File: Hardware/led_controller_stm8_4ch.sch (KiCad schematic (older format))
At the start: 27 parts, among them J1 LEDS, J2 STM8_Prog_Conn, J3 EXT_BTN, Q1 2N7002, Q2 2N7002, Q3 2N7002, Q4 2N7002, SW1 SW_Push, U1 STM8S103F3

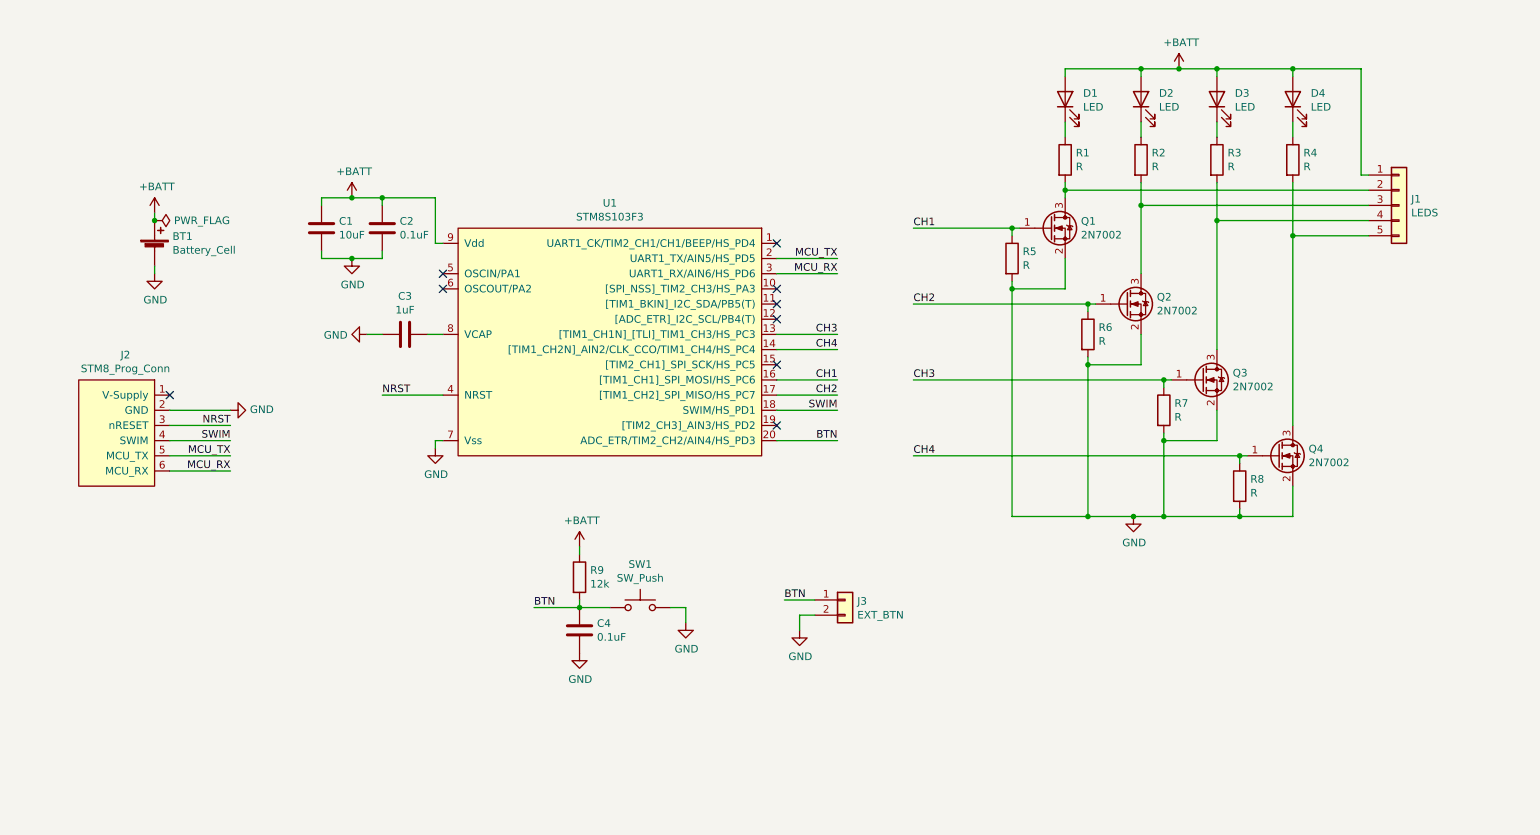
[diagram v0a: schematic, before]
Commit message: add battery protection
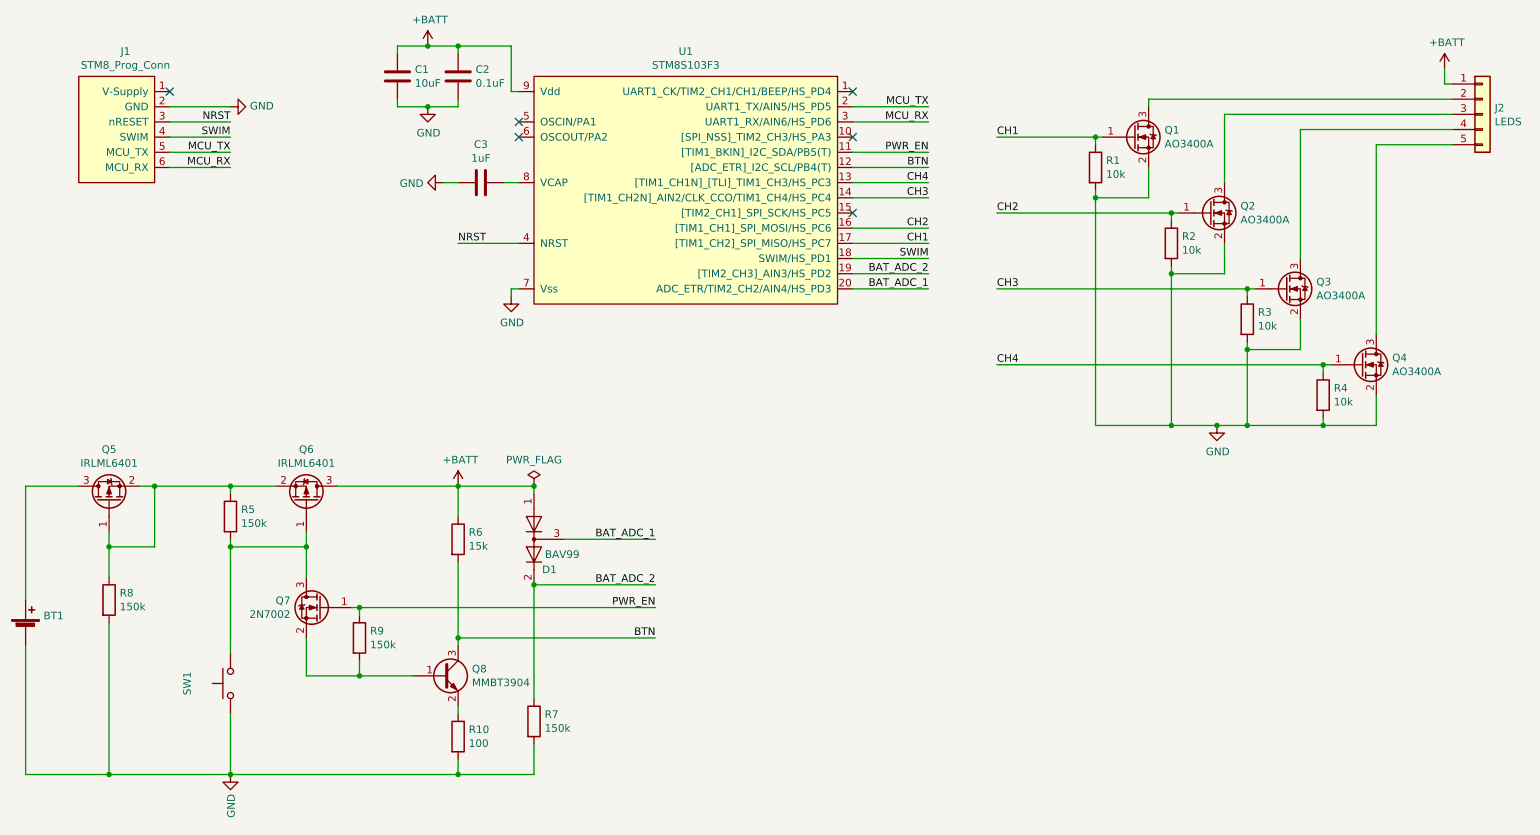
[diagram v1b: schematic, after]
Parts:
- removed C4: 0.1uF, Capacitor_SMD:C_0805_2012Metric_Pad1.15x1.40mm_HandSolder, symbol Device:C
- removed D1, D2, D3, D4: LED, LED_SMD:LED_0805_2012Metric_Pad1.15x1.40mm_HandSolder, symbol Device:LED
- removed J3: EXT_BTN, Connector_JST:JST_PH_B2B-PH-K_1x02_P2.00mm_Vertical, symbol Connector_Generic:Conn_01x02
- removed Q1, Q2, Q3, Q4: 2N7002, Package_TO_SOT_SMD:SOT-23, symbol Transistor_FET:2N7002
- removed R1: R, Resistor_SMD:R_0805_2012Metric_Pad1.15x1.40mm_HandSolder, symbol Device:R
- added D1: BAV99, Package_TO_SOT_SMD:SOT-23, symbol Diode:BAV99
- added Q1, Q2, Q3, Q4: AO3400A, Package_TO_SOT_SMD:SOT-23, symbol Transistor_FET:AO3400A
- added Q5, Q6: IRLML6401, Package_TO_SOT_SMD:SOT-23, symbol Transistor_FET:IRLML6401
- added Q7: 2N7002, Package_TO_SOT_SMD:SOT-23, symbol Transistor_FET:2N7002
- added Q8: MMBT3904, Package_TO_SOT_SMD:SOT-23, symbol Transistor_BJT:MMBT3904
- added R10: 100, Resistor_SMD:R_0805_2012Metric_Pad1.15x1.40mm_HandSolder, symbol Device:R
- added R5: 150k, Resistor_SMD:R_0805_2012Metric_Pad1.15x1.40mm_HandSolder, symbol Device:R
- R1: renamed from R5; value R -> 10k
- R2, R3, R4: value R -> 10k
- R6: value R -> 15k
- R7, R8: value R -> 150k
- R9: value 12k -> 150k
- renumbered J2 to J1, J1 to J2
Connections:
- net +BATT: now also R6.1, D1.1 (K), Q6.3 (D); no longer BT1.1 (+), R9.1
- net BTN: now also R6.2, U1.12 ([ADC_ETR]_I2C_SCL/PB4(T)), Q8.3 (C); no longer R9.2, SW1.1, U1.20 (ADC_ETR/TIM2_CH2/AIN4/HS_PD3)
- net CH1: now also U1.17 ([TIM1_CH2]_SPI_MISO/HS_PC7), Q1.1 (G); no longer U1.16 ([TIM1_CH1]_SPI_MOSI/HS_PC6)
- net CH2: now also R2.1, U1.16 ([TIM1_CH1]_SPI_MOSI/HS_PC6), Q2.1 (G); no longer R6.1, U1.17 ([TIM1_CH2]_SPI_MISO/HS_PC7)
- net CH3: now also R3.1, U1.14 ([TIM1_CH2N]_AIN2/CLK_CCO/TIM1_CH4/HS_PC4), Q3.1 (G); no longer R7.1, U1.13 ([TIM1_CH1N]_[TLI]_TIM1_CH3/HS_PC3)
- net CH4: now also R4.1, U1.13 ([TIM1_CH1N]_[TLI]_TIM1_CH3/HS_PC3), Q4.1 (G); no longer R8.1, U1.14 ([TIM1_CH2N]_AIN2/CLK_CCO/TIM1_CH4/HS_PC4)
- net GND: now also R2.2, R3.2, R4.2, SW1.1, Q1.2 (S), Q2.2 (S), Q3.2 (S), Q4.2 (S), R10.2; no longer R6.2, SW1.2
- net PWR_EN: now reaches U1.11 ([TIM1_BKIN]_I2C_SDA/PB5(T))
- net PWR_EN: now also R9.1, Q7.1 (G)
- net BAT_ADC_2: now reaches U1.19 ([TIM2_CH3]_AIN3/HS_PD2)
- net BAT_ADC_2: now also R7.1, D1.2 (A)
- net at J2.2 (Pin_2): now also Q1.3 (D)
- net at J2.3 (Pin_3): now also Q2.3 (D); no longer R2.2
- net at J2.4 (Pin_4): now also Q3.3 (D); no longer R3.2
- net at J2.5 (Pin_5): now also Q4.3 (D); no longer R4.2
- new net: BT1.1 (+), Q5.3 (D)
- new net: Q6.1 (G), Q7.3 (D), R5.2, SW1.2
- new net: Q5.1 (G), Q5.2 (S), Q6.2 (S), R5.1, R8.1
- new net: Q7.2 (S), Q8.1 (B), R9.2
- new net: Q8.2 (E), R10.1
- new net BAT_ADC_1: D1.3 (K), U1.20 (ADC_ETR/TIM2_CH2/AIN4/HS_PD3)
- no-connect marks 9 -> 6
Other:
- moved on the sheet: BT1, C1, C2, C3, J1, J2, R1, SW1, U1

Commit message: fix PWR_EN pin
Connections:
- net PWR_EN: now also U1.1 (UART1_CK/TIM2_CH1/CH1/BEEP/HS_PD4); no longer U1.11 ([TIM1_BKIN]_I2C_SDA/PB5(T))
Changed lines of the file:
@@
 Wire Wire Line
 	10050 1950 10050 3200
-NoConn ~ 6600 1600
 NoConn ~ 6600 2400
 $Comp
@@
 Wire Wire Line
 	2500 5700 2500 6100
-Text Label 7100 2000 2    50   ~ 0
+Text Label 7100 1600 2    50   ~ 0
 PWR_EN
 Text Label 7100 2800 2    50   ~ 0
@@
 	6600 2800 7100 2800
 Wire Wire Line
-	6600 2000 7100 2000
-Wire Wire Line
 	6600 2100 7100 2100
 Wire Wire Line
@@
 Wire Wire Line
 	4500 5900 4500 6100
+Wire Wire Line
+	6600 1600 7100 1600
+NoConn ~ 6600 2000
 $EndSCHEMATC
